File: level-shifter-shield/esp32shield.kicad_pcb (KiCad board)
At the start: 2 copper layers, 68.6 x 61 mm, 22 parts, among them J1 Power_Terminal, J2 Screw_Terminal_01x02, J3 Screw_Terminal_01x02, J4 Screw_Terminal_01x02, J5 Screw_Terminal_01x02, J6 Conn_01x19_Female, J7 Conn_01x19_Female, J8 Conn_02x19_Counter_Clockwise, U2 74HC245

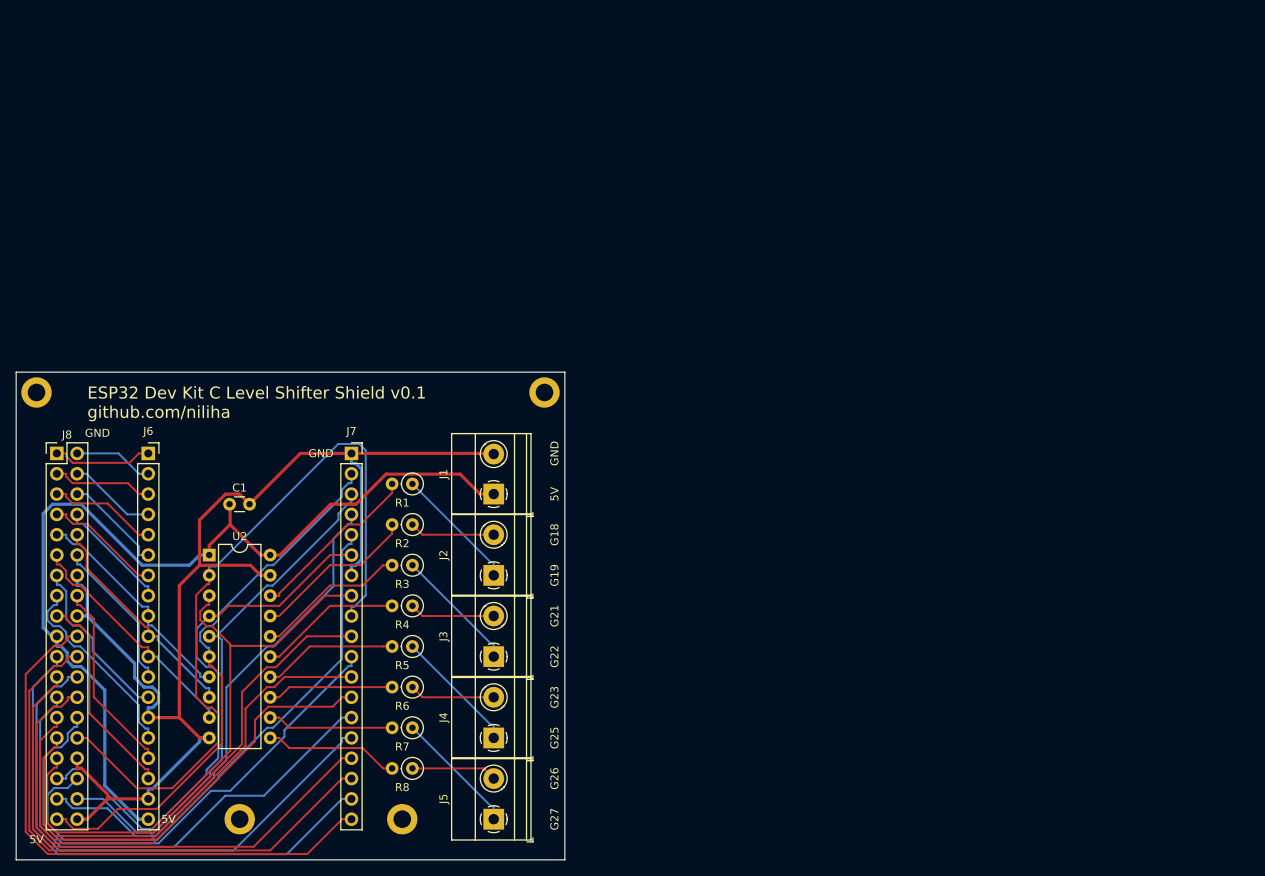
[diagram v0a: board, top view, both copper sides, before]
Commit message: Finish level shifter shield layout without traces
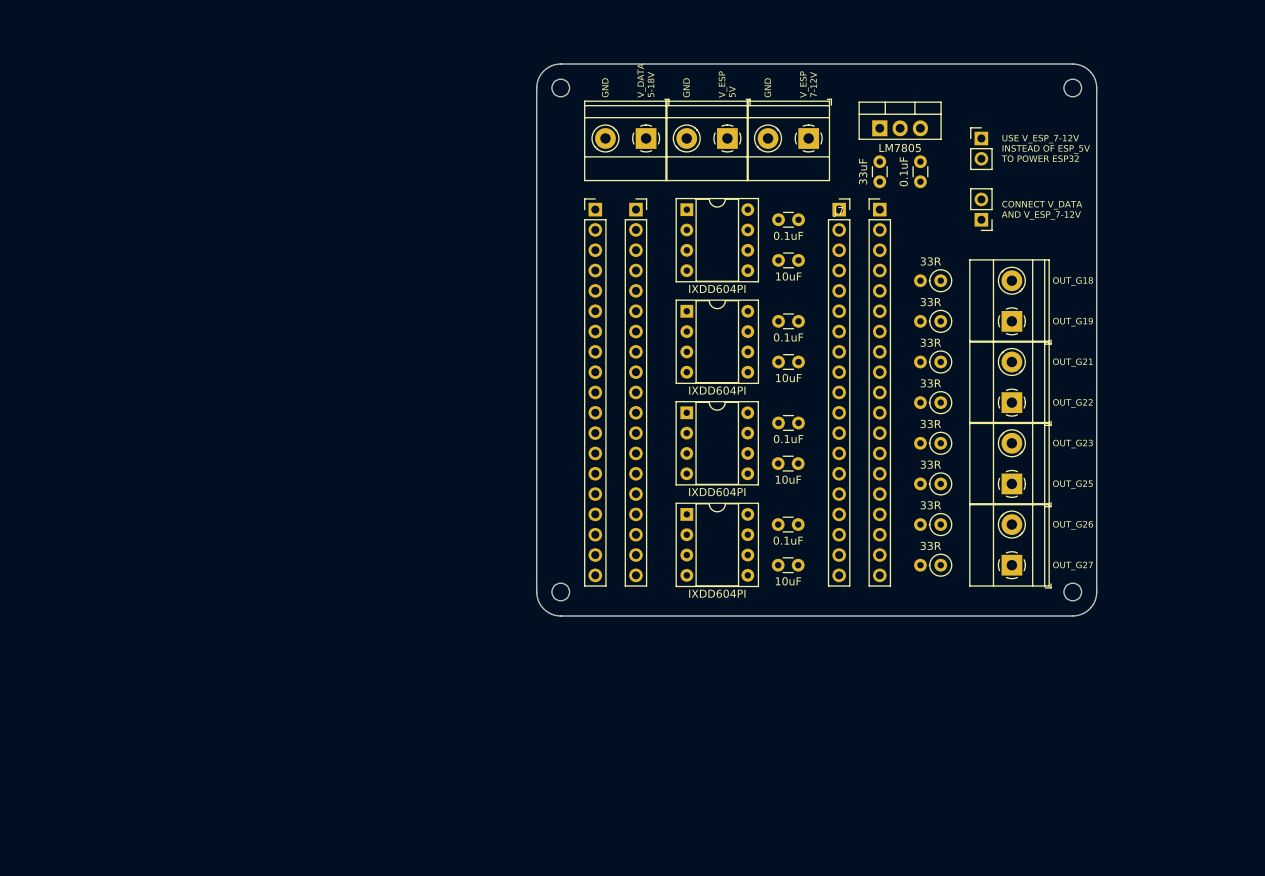
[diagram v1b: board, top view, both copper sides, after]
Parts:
- added C10: 10uF, Capacitor_THT:C_Disc_D3.0mm_W1.6mm_P2.50mm, F.Cu at (170.2, 120.7)
- added C2: 0.1uF, Capacitor_THT:C_Disc_D3.0mm_W1.6mm_P2.50mm, F.Cu at (188.0, 70.2)
- added C3: 0.1uF, Capacitor_THT:C_Disc_D3.0mm_W1.6mm_P2.50mm, F.Cu at (170.2, 77.5)
- added C4: 0.1uF, Capacitor_THT:C_Disc_D3.0mm_W1.6mm_P2.50mm, F.Cu at (170.2, 90.2)
- added C5: 0.1uF, Capacitor_THT:C_Disc_D3.0mm_W1.6mm_P2.50mm, F.Cu at (170.2, 102.9)
- added C6: 0.1uF, Capacitor_THT:C_Disc_D3.0mm_W1.6mm_P2.50mm, F.Cu at (170.2, 115.6)
- added C7: 10uF, Capacitor_THT:C_Disc_D3.0mm_W1.6mm_P2.50mm, F.Cu at (170.2, 82.5)
- added C8: 10uF, Capacitor_THT:C_Disc_D3.0mm_W1.6mm_P2.50mm, F.Cu at (170.2, 95.2)
- added C9: 10uF, Capacitor_THT:C_Disc_D3.0mm_W1.6mm_P2.50mm, F.Cu at (170.2, 108.0)
- added J10: Screw_Terminal_01x02, TerminalBlock_Phoenix:TerminalBlock_Phoenix_MKDS-1,5-2-5.08_1x02_P5.08mm_Horizontal, F.Cu at (199.4, 90.2)
- added J11: Screw_Terminal_01x02, TerminalBlock_Phoenix:TerminalBlock_Phoenix_MKDS-1,5-2-5.08_1x02_P5.08mm_Horizontal, F.Cu at (199.4, 110.5)
- added J9: Screw_Terminal_01x02, TerminalBlock_Phoenix:TerminalBlock_Phoenix_MKDS-1,5-2-5.08_1x02_P5.08mm_Horizontal, F.Cu at (199.4, 120.7)
- added JP1: Jumper_2_Open, Connector_PinHeader_2.54mm:PinHeader_1x02_P2.54mm_Vertical, F.Cu at (195.6, 77.5)
- added JP2: Jumper_2_Open, Connector_PinHeader_2.54mm:PinHeader_1x02_P2.54mm_Vertical, F.Cu at (195.6, 67.3)
- added U1: LM7805, Package_TO_SOT_THT:TO-220-3_Vertical, F.Cu at (182.9, 66.0)
- added U3: IXDD604PI, Package_DIP:DIP-8_W7.62mm_Socket, F.Cu at (158.8, 88.9)
- added U4: IXDD604PI, Package_DIP:DIP-8_W7.62mm_Socket, F.Cu at (158.8, 101.6)
- added U5: IXDD604PI, Package_DIP:DIP-8_W7.62mm_Socket, F.Cu at (158.8, 114.3)
- C1: value 0.1u -> 33uF
- H1, H2, H3, H4: value MountingHole_2.2mm_M2_DIN965_Pad -> MountingHole; footprint MountingHole:MountingHole_2.2mm_M2_DIN965_Pad -> MountingHole:MountingHole_2.2mm_M2
- J1: footprint TerminalBlock_Phoenix:TerminalBlock_Phoenix_MKDS-1,5-2_1x02_P5.00mm_Horizontal -> TerminalBlock_Phoenix:TerminalBlock_Phoenix_MKDS-1,5-2-5.08_1x02_P5.08mm_Horizontal
- J2: value Screw_Terminal_01x02 -> Conn_01x19_Pin; footprint TerminalBlock_Phoenix:TerminalBlock_Phoenix_MKDS-1,5-2-5.08_1x02_P5.08mm_Horizontal -> Connector_PinHeader_2.54mm:PinHeader_1x19_P2.54mm_Vertical
- J3, J5: value Screw_Terminal_01x02 -> Power_Terminal
- J4: value Screw_Terminal_01x02 -> Conn_01x19_Socket; footprint TerminalBlock_Phoenix:TerminalBlock_Phoenix_MKDS-1,5-2-5.08_1x02_P5.08mm_Horizontal -> Connector_PinSocket_2.54mm:PinSocket_1x19_P2.54mm_Vertical
- J6: value Conn_01x19_Female -> Conn_01x19_Socket
- J7: value Conn_01x19_Female -> Conn_01x19_Pin; footprint Connector_PinSocket_2.54mm:PinSocket_1x19_P2.54mm_Vertical -> Connector_PinHeader_2.54mm:PinHeader_1x19_P2.54mm_Vertical
- J8: value Conn_02x19_Counter_Clockwise -> Screw_Terminal_01x02; footprint Connector_PinHeader_2.54mm:PinHeader_2x19_P2.54mm_Vertical -> TerminalBlock_Phoenix:TerminalBlock_Phoenix_MKDS-1,5-2-5.08_1x02_P5.08mm_Horizontal
- R1, R2, R3, R4, R5, R6, R7, R8: value 220 -> 33R
- U2: value 74HC245 -> IXDD604PI; footprint Package_DIP:DIP-20_W7.62mm -> Package_DIP:DIP-8_W7.62mm_Socket
- moved J8 119.5 mm to (199.4, 100.3), turned to 90 degrees
- moved J5 93.8 mm to (174.0, 67.3), turned to 180 degrees
- moved C1 91.9 mm to (182.9, 70.2), turned to -90 degrees
- moved J6 91.6 mm to (177.8, 76.2)
- moved H3 88.5 mm to (207.0, 124.0)
- moved R5 80.3 mm to (190.5, 85.1)
- moved R6 80.3 mm to (190.5, 90.2)
- moved H2 76.2 mm to (207.0, 61.0)
- moved H1 75.8 mm to (143.0, 61.0)
- moved R7 75.0 mm to (190.5, 105.4)
- moved R8 75.0 mm to (190.5, 110.5)
- moved U2 73.7 mm to (158.8, 76.2)
- moved J7 72.7 mm to (182.9, 76.2)
- moved J3 71.1 mm to (163.8, 67.3), turned to 180 degrees
- moved J4 68.4 mm to (152.4, 76.2), turned to 0 degrees
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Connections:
- C1 pad 1: +5V -> V_ESP_7-12V
- J1 pad 1: +5V -> V_DATA
- J2 pad 1: Net-(J2-Pad1) -> /3V3
- J2 pad 2: Net-(J2-Pad2) -> /EN
- J3 pad 1: Net-(J3-Pad1) -> V_ESP_5V
- J3 pad 2: Net-(J3-Pad2) -> GND
- J4 pad 1: Net-(J4-Pad1) -> /3V3
- J4 pad 2: Net-(J4-Pad2) -> /EN
- J5 pad 1: Net-(J5-Pad1) -> V_ESP_7-12V
- J5 pad 2: Net-(J5-Pad2) -> GND
- J6 pad 1: /3V3 -> GND
- J6 pad 10: /G26 -> /G5
- J6 pad 11: /G27 -> /G17
- J6 pad 12: /G14 -> /G16
- J6 pad 13: /G12 -> /G4
- J6 pad 14: GND -> /G0
- J6 pad 15: /G13 -> /G2
- J6 pad 16: /SD2 -> /G15
- J6 pad 17: /SD3 -> /SD1
- J6 pad 18: GND -> /SD0
- J6 pad 19: +5V -> /CLK
- J6 pad 2: /EN -> /G23
- J6 pad 3: /SP -> /G22
- J6 pad 4: /SN -> /TXD
- J6 pad 5: /G34 -> /RXD
- J6 pad 6: /G35 -> /G21
- J6 pad 7: /G32 -> GND
- J6 pad 8: /G33 -> /G19
- J6 pad 9: /G25 -> /G18
- J8 pad 1: /3V3 -> /OUT_G22_TERM
- J8 pad 2: /EN -> /OUT_G21_TERM
- R1 pad 1: Net-(J2-Pad1) -> /OUT_G21_TERM
- R1 pad 2: Net-(R1-Pad2) -> /OUT_G21
- R2 pad 1: Net-(J2-Pad2) -> /OUT_G22_TERM
- R2 pad 2: Net-(R2-Pad2) -> /OUT_G22
- R3 pad 1: Net-(J3-Pad1) -> /OUT_G26_TERM
- R3 pad 2: Net-(R3-Pad2) -> /OUT_G26
- R4 pad 1: Net-(J3-Pad2) -> /OUT_G27_TERM
- R4 pad 2: Net-(R4-Pad2) -> /OUT_G27
- R5 pad 1: Net-(J4-Pad1) -> /OUT_G18_TERM
- R5 pad 2: Net-(R5-Pad2) -> /OUT_G18
- R6 pad 1: Net-(J4-Pad2) -> /OUT_G19_TERM
- R6 pad 2: Net-(R6-Pad2) -> /OUT_G19
- R7 pad 1: Net-(J5-Pad1) -> /OUT_G23_TERM
- R7 pad 2: Net-(R7-Pad2) -> /OUT_G23
- R8 pad 1: Net-(J5-Pad2) -> /OUT_G25_TERM
- R8 pad 2: Net-(R8-Pad2) -> /OUT_G25
- U2 pad 1: +5V -> unconnected-(U2-ENA-Pad1)
- U2 pad 3: /G19 -> GND
- U2 pad 4: /G21 -> /G19
- U2 pad 5: /G22 -> /OUT_G19
- U2 pad 6: /G23 -> V_DATA
- U2 pad 7: /G25 -> /OUT_G18
- U2 pad 8: /G26 -> unconnected-(U2-ENB-Pad8)
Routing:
- net GND: track 155.7 -> 0.00 mm
- net +5V: track 118.1 -> 0.00 mm
- net /G18: track 94.9 -> 0.00 mm
- net /G19: track 76.1 -> 0.00 mm
- net /CLK: track 72.0 -> 0.00 mm
- net /RXD: track 71.5 -> 0.00 mm
- net /SD1: track 70.4 -> 0.00 mm
- net /G23: track 69.8 -> 0.00 mm
- net /G4: track 68.9 -> 0.00 mm
- net /G21: track 68.9 -> 0.00 mm
- net /G2: track 68.8 -> 0.00 mm
- net /SD0: track 67.0 -> 0.00 mm
- net /G17: track 66.1 -> 0.00 mm
- net /G22: track 66.0 -> 0.00 mm
- net /G15: track 65.8 -> 0.00 mm
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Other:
- board size 68.6 x 61 mm -> 70 x 69 mm
- net class Default removed
- net class Supply removed
- board text added: "CONNECT V_DATA AND V_ESP_7-12V"
- board text added: "OUT_G18"
- board text added: "OUT_G19"
- board text added: "OUT_G21"
- board text added: "OUT_G22"
- board text added: "OUT_G23"
- board text added: "OUT_G25"
- board text added: "OUT_G26"
- board text added: "OUT_G27"
- board text added: "USE V_ESP_7-12V INSTEAD OF ESP_5V TO POWER ESP32"
- board text added: "V_DATA 5-18V"
- board text added: "V_ESP 5V"
- board text added: "V_ESP 7-12V"
- board text removed: "5V"
- board text removed: "ESP32 Dev Kit C Level Shifter Shield v0.1 github.com/niliha"
- board text removed: "G18"
- board text removed: "G19"
- board text removed: "G21"
- board text removed: "G22"
- board text removed: "G23"
- board text removed: "G25"
- board text removed: "G26"
- board text removed: "G27"

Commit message: Adapt level shifter shield layout and add routing
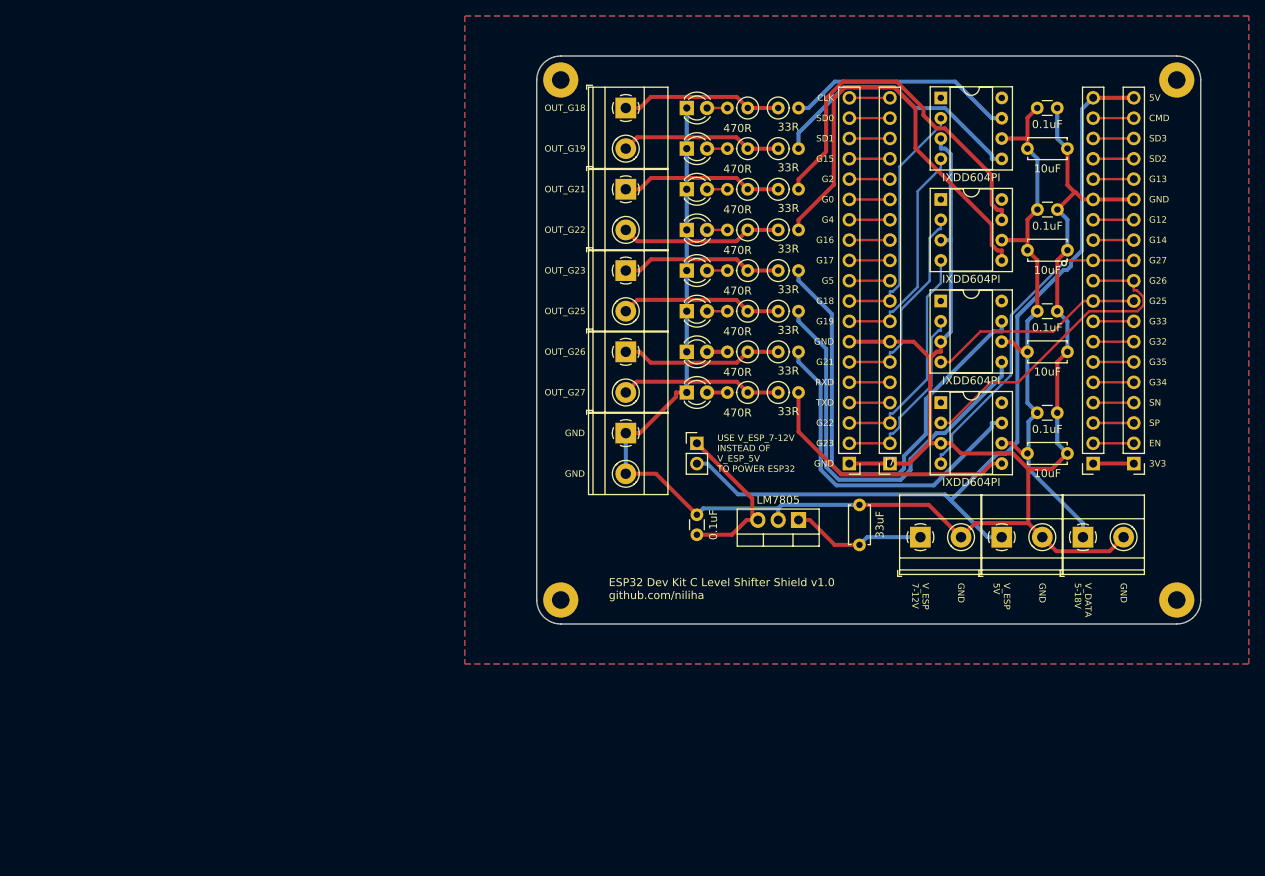
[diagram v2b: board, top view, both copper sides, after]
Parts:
- removed JP2: Jumper_2_Open, Connector_PinHeader_2.54mm:PinHeader_1x02_P2.54mm_Vertical
- added D1: RED, LED_THT:LED_D3.0mm, F.Cu at (158.8, 63.5)
- added D2: RED, LED_THT:LED_D3.0mm, F.Cu at (158.8, 68.6)
- added D3: RED, LED_THT:LED_D3.0mm, F.Cu at (158.8, 73.7)
- added D4: RED, LED_THT:LED_D3.0mm, F.Cu at (158.8, 78.7)
- added D5: RED, LED_THT:LED_D3.0mm, F.Cu at (158.8, 83.8)
- added D6: RED, LED_THT:LED_D3.0mm, F.Cu at (158.8, 88.9)
- added D7: RED, LED_THT:LED_D3.0mm, F.Cu at (158.8, 94.0)
- added D8: RED, LED_THT:LED_D3.0mm, F.Cu at (158.8, 99.1)
- added J12: Screw_Terminal_01x02, TerminalBlock_Phoenix:TerminalBlock_Phoenix_MKDS-1,5-2-5.08_1x02_P5.08mm_Horizontal, F.Cu at (151.1, 94.0)
- added R10: 470R, Resistor_THT:R_Axial_DIN0207_L6.3mm_D2.5mm_P2.54mm_Vertical, F.Cu at (166.4, 73.7)
- added R11: 470R, Resistor_THT:R_Axial_DIN0207_L6.3mm_D2.5mm_P2.54mm_Vertical, F.Cu at (166.4, 78.7)
- added R12: 470R, Resistor_THT:R_Axial_DIN0207_L6.3mm_D2.5mm_P2.54mm_Vertical, F.Cu at (166.4, 83.8)
- added R13: 470R, Resistor_THT:R_Axial_DIN0207_L6.3mm_D2.5mm_P2.54mm_Vertical, F.Cu at (166.4, 68.6)
- added R14: 470R, Resistor_THT:R_Axial_DIN0207_L6.3mm_D2.5mm_P2.54mm_Vertical, F.Cu at (166.4, 88.9)
- added R15: 470R, Resistor_THT:R_Axial_DIN0207_L6.3mm_D2.5mm_P2.54mm_Vertical, F.Cu at (166.4, 94.0)
- added R16: 470R, Resistor_THT:R_Axial_DIN0207_L6.3mm_D2.5mm_P2.54mm_Vertical, F.Cu at (166.4, 99.1)
- added R9: 470R, Resistor_THT:R_Axial_DIN0207_L6.3mm_D2.5mm_P2.54mm_Vertical, F.Cu at (166.4, 63.5)
- C1, C10, C7, C8, C9: footprint Capacitor_THT:C_Disc_D3.0mm_W1.6mm_P2.50mm -> Capacitor_THT:C_Disc_D4.7mm_W2.5mm_P5.00mm
- H1, H2, H3, H4: footprint MountingHole:MountingHole_2.2mm_M2 -> MountingHole:MountingHole_2.2mm_M2_Pad
- J8: value Screw_Terminal_01x02 -> Power_Terminal
- moved J9 74.8 mm to (151.1, 63.5), turned to -90 degrees
- moved J2 74.4 mm to (214.6, 108.0), turned to 180 degrees
- moved J1 73.9 mm to (208.3, 117.1), turned to 0 degrees
- moved J4 65.4 mm to (209.6, 108.0), turned to 180 degrees
- moved J3 60.5 mm to (198.1, 117.1), turned to 0 degrees
- moved J11 55.1 mm to (151.1, 83.8), turned to -90 degrees
- moved C2 54.4 mm to (160.0, 116.8), turned to 90 degrees
- moved J5 51.8 mm to (188.0, 117.1), turned to 0 degrees
- moved J10 51.0 mm to (151.1, 73.7), turned to -90 degrees
- moved U1 50.0 mm to (172.7, 115.0), turned to 180 degrees
- moved J8 48.4 mm to (151.1, 104.1), turned to -90 degrees
- moved C1 48.0 mm to (180.3, 118.1), turned to 90 degrees
- moved R4 46.6 mm to (170.2, 78.7), turned to 0 degrees
- moved R3 46.6 mm to (170.2, 73.7), turned to 0 degrees
- moved JP1 45.2 mm to (160.0, 105.4), turned to 0 degrees
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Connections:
- J10 pad 1: /OUT_G19_TERM -> /OUT_G21_TERM
- J10 pad 2: /OUT_G18_TERM -> /OUT_G22_TERM
- J11 pad 1: /OUT_G25_TERM -> /OUT_G23_TERM
- J11 pad 2: /OUT_G23_TERM -> /OUT_G25_TERM
- J8 pad 1: /OUT_G22_TERM -> GND
- J8 pad 2: /OUT_G21_TERM -> GND
- J9 pad 1: /OUT_G27_TERM -> /OUT_G18_TERM
- J9 pad 2: /OUT_G26_TERM -> /OUT_G19_TERM
- JP1 pad 1: V_DATA -> /5V_OUT_REG
- JP1 pad 2: V_ESP_7-12V -> V_ESP_5V
- R1 pad 1: /OUT_G21_TERM -> /OUT_G18_TERM
- R1 pad 2: /OUT_G21 -> /OUT_G18
- R2 pad 1: /OUT_G22_TERM -> /OUT_G19_TERM
- R2 pad 2: /OUT_G22 -> /OUT_G19
- R3 pad 1: /OUT_G26_TERM -> /OUT_G21_TERM
- R3 pad 2: /OUT_G26 -> /OUT_G21
- R4 pad 1: /OUT_G27_TERM -> /OUT_G22_TERM
- R4 pad 2: /OUT_G27 -> /OUT_G22
- R5 pad 1: /OUT_G18_TERM -> /OUT_G23_TERM
- R5 pad 2: /OUT_G18 -> /OUT_G23
- R6 pad 1: /OUT_G19_TERM -> /OUT_G25_TERM
- R6 pad 2: /OUT_G19 -> /OUT_G25
- R7 pad 1: /OUT_G23_TERM -> /OUT_G26_TERM
- R7 pad 2: /OUT_G23 -> /OUT_G26
- R8 pad 1: /OUT_G25_TERM -> /OUT_G27_TERM
- R8 pad 2: /OUT_G25 -> /OUT_G27
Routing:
- net GND: track 0.00 -> 266.7 mm
- net V_ESP_5V: track 0.00 -> 105.5 mm
- net V_DATA: track 0.00 -> 74.0 mm
- net /OUT_G23: track 0.00 -> 59.9 mm
- net /OUT_G22: track 0.00 -> 53.9 mm
- net /OUT_G25: track 0.00 -> 51.4 mm
- net /OUT_G21: track 0.00 -> 46.1 mm
- net /OUT_G26: track 0.00 -> 42.9 mm
- net /G27: track 0.00 -> 40.5 mm, vias 0 -> 1
- net /G26: track 0.00 -> 40.3 mm
- net /OUT_G19: track 0.00 -> 33.7 mm
- net /OUT_G27: track 0.00 -> 33.1 mm
- net /G18: track 0.00 -> 30.9 mm
- net /OUT_G18: track 0.00 -> 28.7 mm
- net /G22: track 0.00 -> 28.2 mm
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- added copper zone on B.Cu, net GND
- added copper zone on F.Cu, net GND
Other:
- board size 70 x 69 mm -> 83 x 71 mm
- board text added: "3V3"
- board text added: "5V"
- board text added: "CLK"
- board text added: "CMD"
- board text added: "EN"
- board text added: "ESP32 Dev Kit C Level Shifter Shield v1.0 github.com/niliha"
- board text added: "G0"
- board text added: "G12"
- board text added: "G13"
- board text added: "G14"
- board text added: "G15"
- board text added: "G16"
- board text added: "G17"
- board text added: "G18"
- board text added: "G19"
- board text added: "G2"
- board text added: "G21"
- board text added: "G22"
- board text added: "G23"
- board text added: "G25"
- board text added: "G26"
- board text added: "G27"
- board text added: "G32"
- board text added: "G33"
- board text added: "G34"
- board text added: "G35"
- board text added: "G4"
- board text added: "G5"
- board text added: "RXD"
- board text added: "SD0"
- board text added: "SD1"
- board text added: "SD2"
- board text added: "SD3"
- board text added: "SN"
- board text added: "SP"
- board text added: "TXD"
- board text added: "USE V_ESP_7-12V INSTEAD OF V_ESP_5V TO POWER ESP32"
- board text removed: "CONNECT V_DATA AND V_ESP_7-12V"
- board text removed: "USE V_ESP_7-12V INSTEAD OF ESP_5V TO POWER ESP32"
